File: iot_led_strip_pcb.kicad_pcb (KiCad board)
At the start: 2 copper layers, 50 x 50 mm, 61 parts, among them J1 I2C Expansion, J2 Conn_01x03_Socket, J3 GT-USB-7010ASV, J4 Barrel_Jack_Switch_Pin3Ring, J5 TC2050-IDC_Cortex-M, J6 Conn_01x03_Socket_Solderwire, Q1 BSS138, SW1 RESET, SW2 FLASH, U1 AMS1117-3.3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

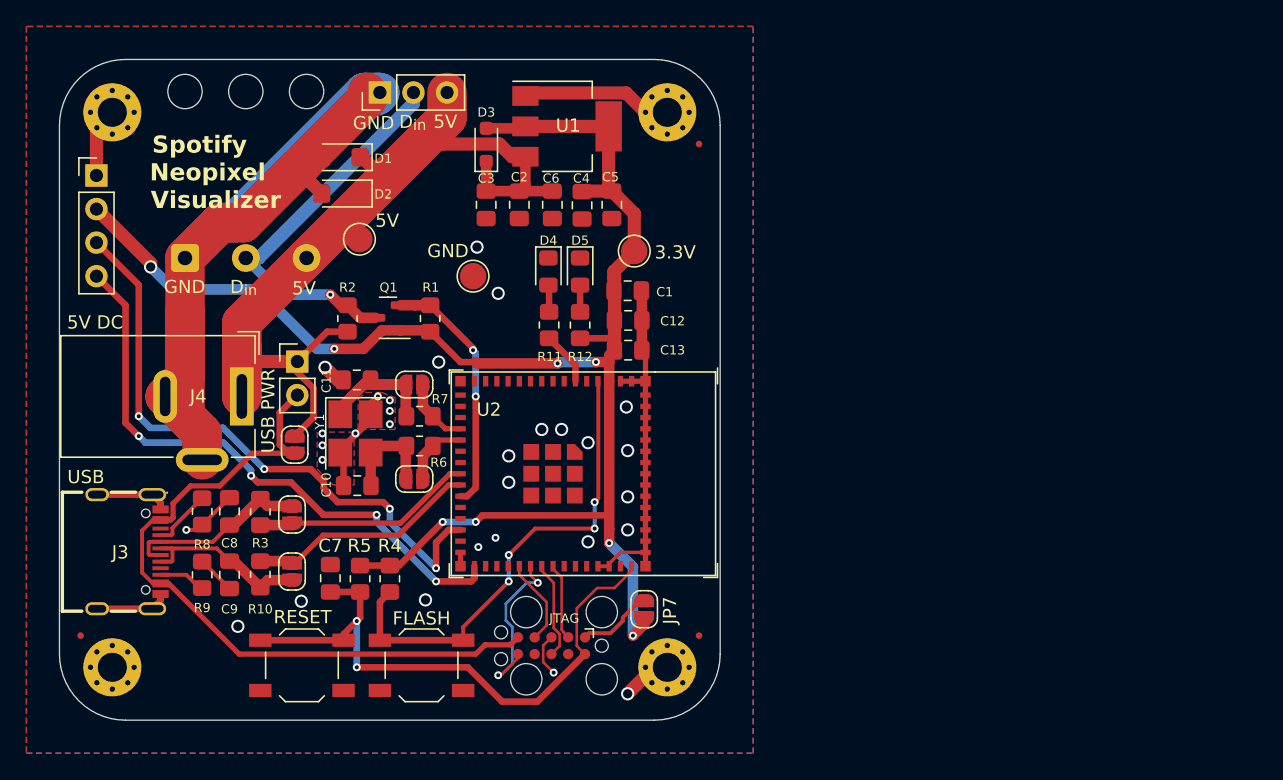
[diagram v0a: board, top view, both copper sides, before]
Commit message: some minor cleanup of schematic and layout
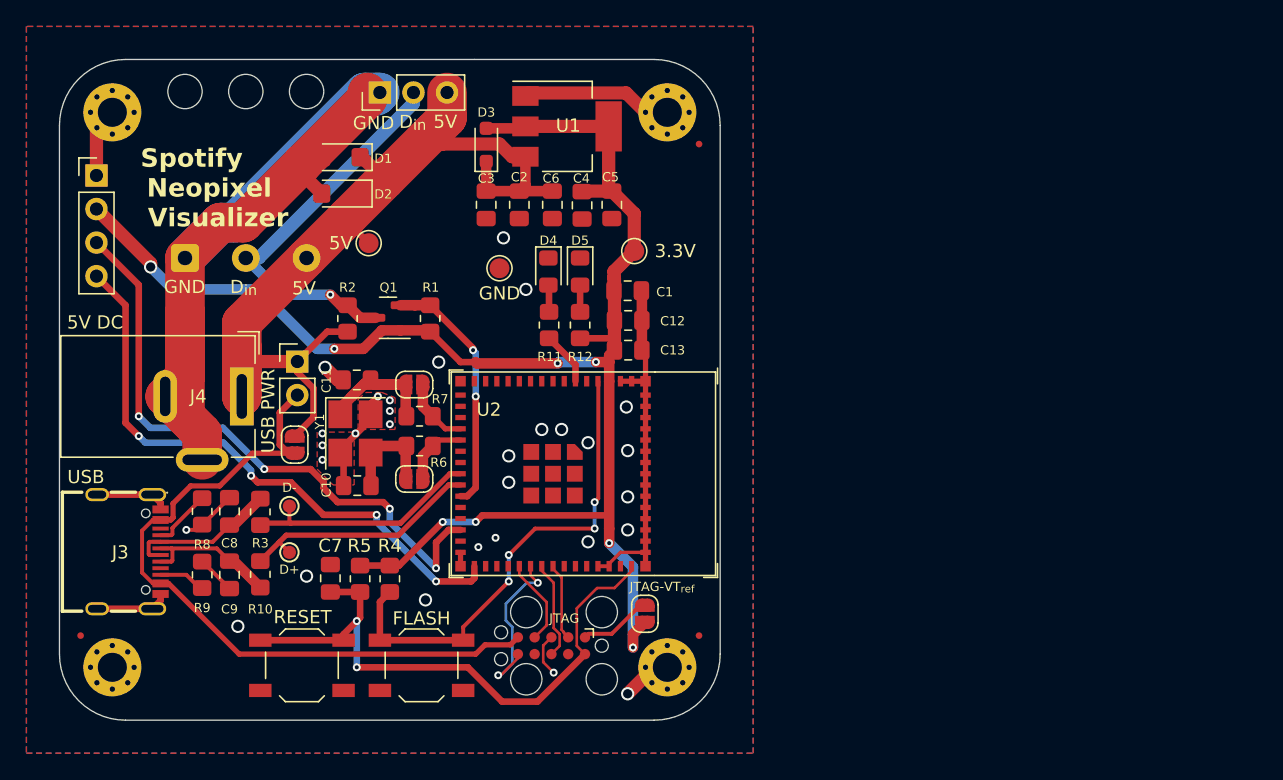
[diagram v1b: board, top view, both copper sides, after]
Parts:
- removed JP2, JP5: SolderJumper_2_Open, Jumper:SolderJumper-2_P1.3mm_Open_RoundedPad1.0x1.5mm
- added TP4: D+, TestPoint:TestPoint_Pad_D1.0mm, F.Cu at (127.4, 107.3)
- added TP5: D-, TestPoint:TestPoint_Pad_D1.0mm, F.Cu at (127.4, 103.8)
- JP7: value JTAG-VTREF -> JTAG-VT_{ref}
- TP1, TP2, TP3: footprint TestPoint:TestPoint_Pad_D2.0mm -> TestPoint:TestPoint_Pad_D1.5mm
- moved TP3 2.09 mm to (143.3, 85.8)
- moved TP1 0.76 mm to (133.4, 83.9)
- moved JP7 0.35 mm to (154.3, 112.0)
- moved REF** 0.28 mm to (123.8, 115.8)
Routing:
- net /DP: track 13.6 -> 10.7 mm
- net /DN: track 14.4 -> 11.6 mm
- net +5V: track 69.7 -> 72.4 mm
- net +3.3V: track 128.8 -> 130.2 mm
- net /USB_D-: track 16.8 -> 18.1 mm
- net /USB_D+: track 17.7 -> 18.6 mm

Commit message: final modifications, cleanup, added v2.0 photos as ordered
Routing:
- net Earth: track 146.6 -> 151.6 mm
- net +5V: track 72.4 -> 75.4 mm
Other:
- board text added: "JTAG VT_{ref}"
- board text added: "v2.0 09-2023"
- board text removed: "v2.0-a 09-2023"

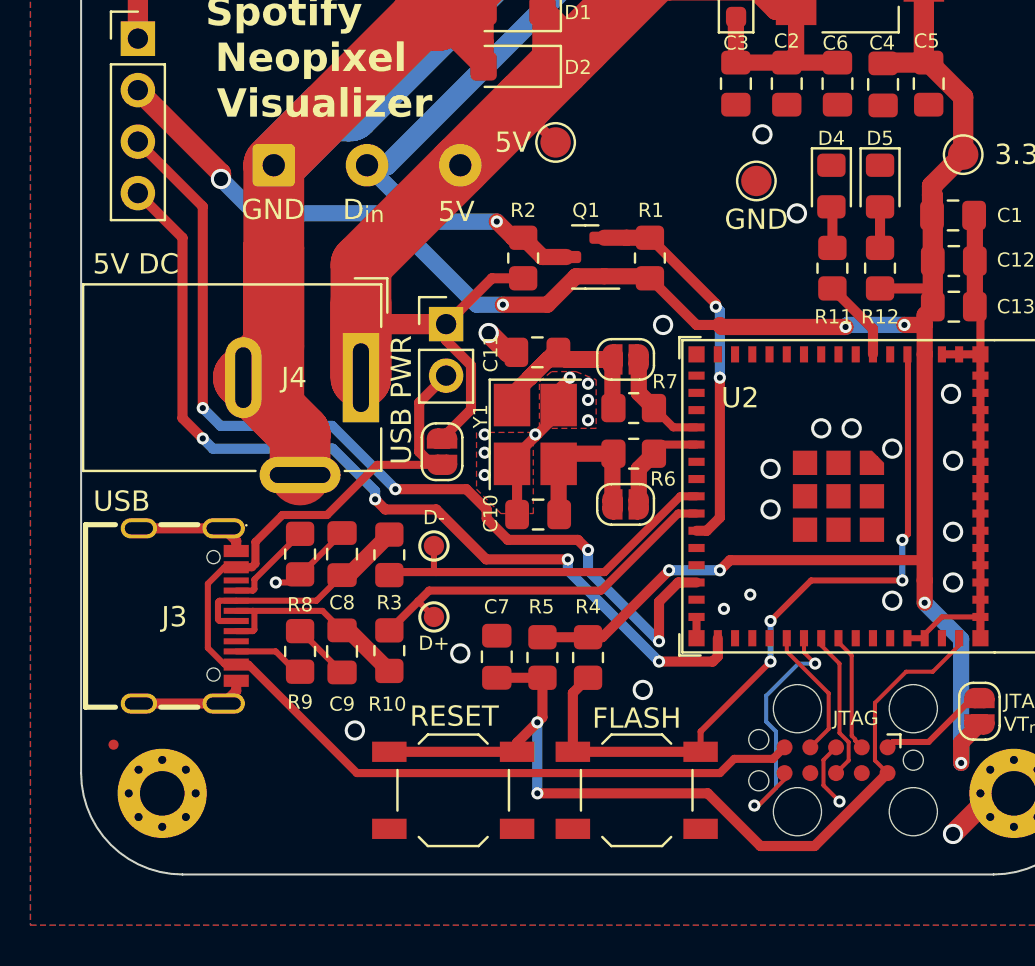
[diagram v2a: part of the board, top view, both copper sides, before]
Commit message: Moved button labels and multiple minor modifications
* Implemented Orion's suggestion for replacing 10uF cap on reset button
  with 100nF.
* Moved silkscreen for both buttons underneath and moved jtag label.
* Added labels to both power and status LEDs.
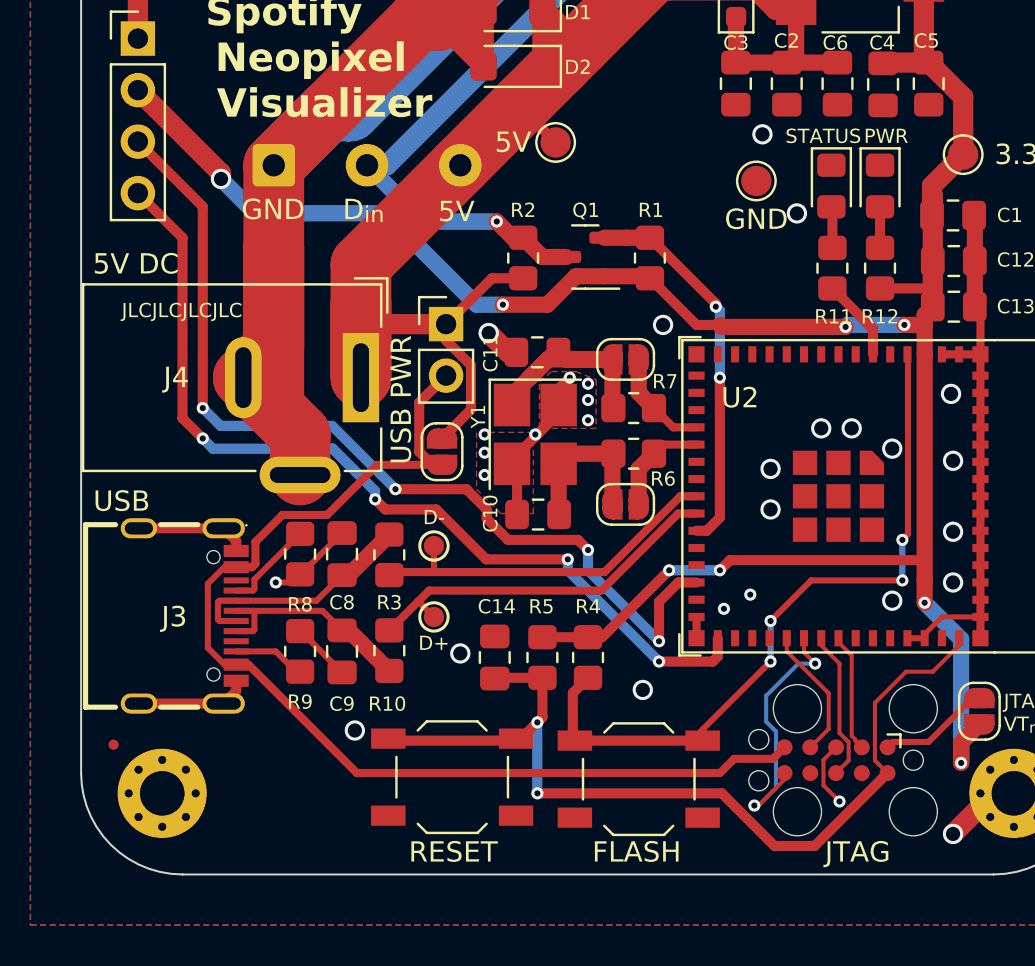
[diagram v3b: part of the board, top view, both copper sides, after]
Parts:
- removed C7: 10uF, Capacitor_SMD:C_0805_2012Metric_Pad1.18x1.45mm_HandSolder
- removed REF**: KiCad-Logo2_5mm_SilkScreen, Symbol:KiCad-Logo2_5mm_SilkScreen
- added C14: 100nF, Capacitor_SMD:C_0805_2012Metric_Pad1.18x1.45mm_HandSolder, F.Cu at (130.4, 109.3)
- D4: value LED -> STATUS
- D5: value PWR_LED -> PWR
- moved SW1 0.65 mm to (128.3, 115.2)
- moved SW2 0.56 mm to (137.5, 115.3)
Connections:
- net /BOOT renamed BOOT
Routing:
- net BOOT: track 36.7 -> 34.9 mm
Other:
- board text added: "JLCJLCJLCJLC"

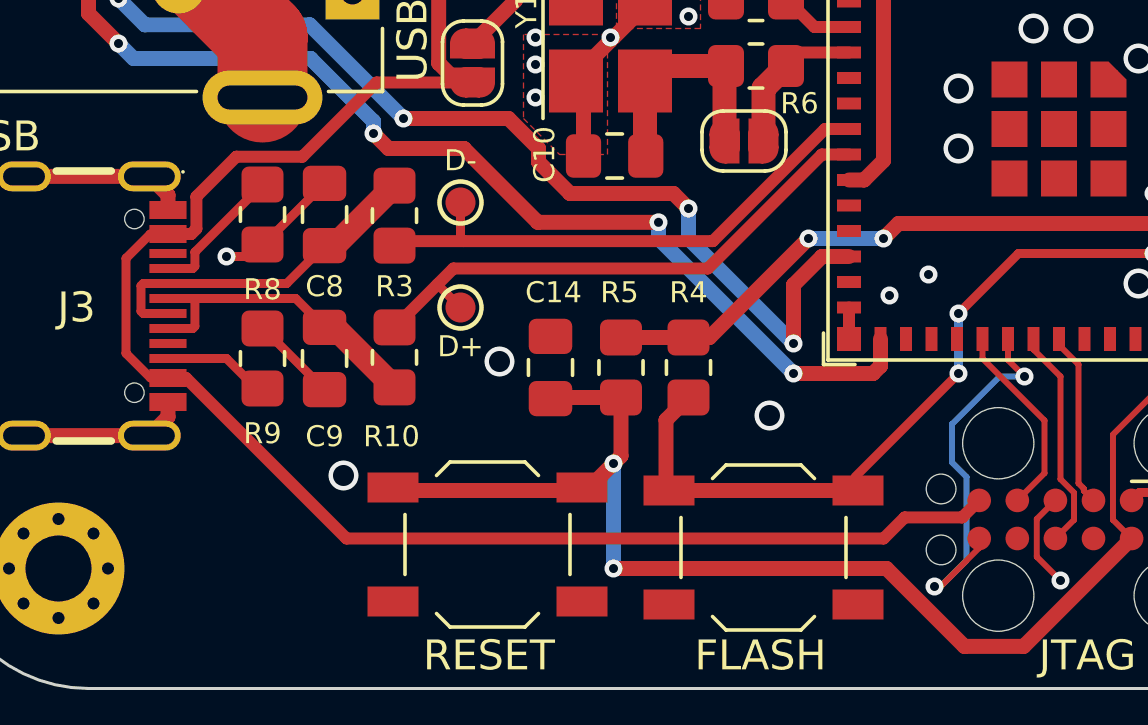
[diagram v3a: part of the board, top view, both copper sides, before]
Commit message: some pcb changes and update to readme
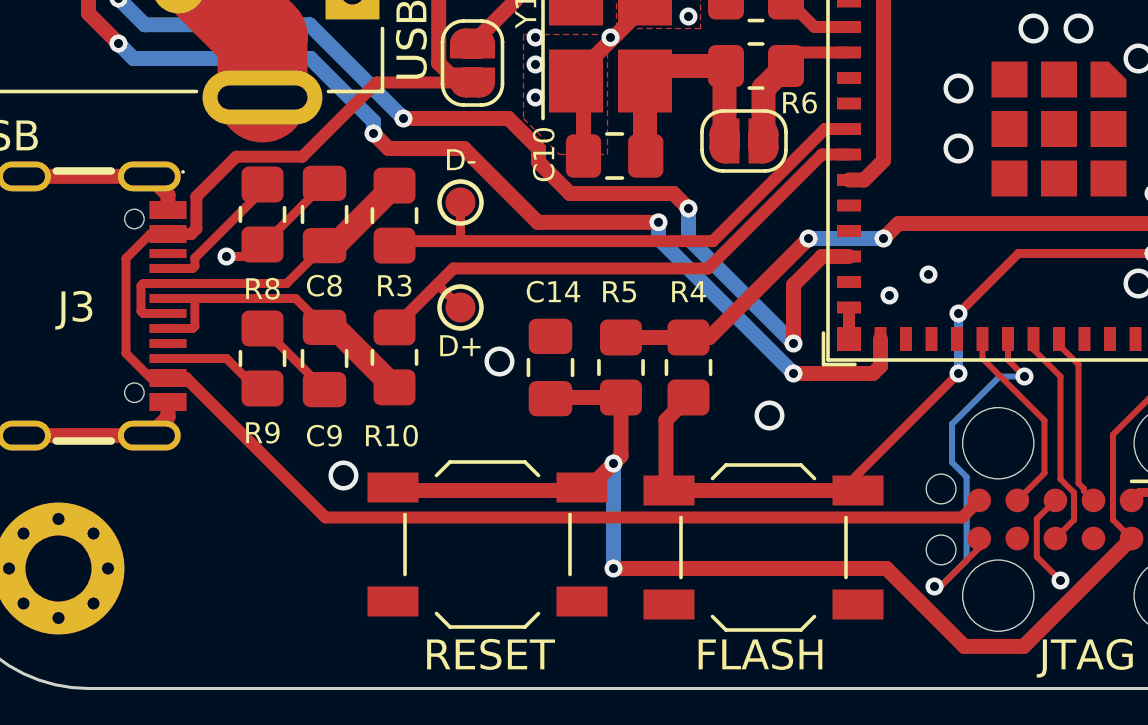
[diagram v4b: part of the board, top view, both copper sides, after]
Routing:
- net VBUS: track 55.0 -> 54.4 mm
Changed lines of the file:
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@@
     (property "Vendor" "https://www.lcsc.com/product-detail/USB-Connectors_G-Switch-GT-USB-7010ASV_C2988369.html")
     (property "ki_keywords" "C2988369")
+    (clearance 0.1)
     (attr smd)
     (fp_text reference "J3" (at 0.05 0.65) (layer "F.SilkS")
@@
     (fp_circle (center 2.889992 -1.280137) (end 3.014986 -1.280137)
       (stroke (width 0.250012) (type solid)) (fill none) (layer "F.Fab"))
-    (pad "" np_thru_hole circle (at -2.899949 -1.280137 270) (size 0.649987 0.649987) (drill 0.649987) (layers "*.Cu" "*.Mask"))
+    (pad "" np_thru_hole circle (at -2.899949 -1.280137 270) (size 0.649987 0.649987) (drill 0.649987) (layers "F&B.Cu" "*.Mask")
+      (clearance 0.1))
     (pad "" np_thru_hole circle (at 2.889992 -1.280137 270) (size 0.649987 0.649987) (drill 0.649987) (layers "*.Cu" "*.Mask"))
     (pad "1" thru_hole oval (at -4.320066 -1.78001 270) (size 1 2.1) (drill oval 0.6 1.7) (layers "*.Cu" "*.Mask")
@@
   (via (at 132.5 112.5) (size 0.6) (drill 0.3) (layers "F.Cu" "B.Cu") (net 6))
   (segment (start 132.5 112.5) (end 132.5 116) (width 0.5) (layer "B.Cu") (net 6))
+  (segment (start 118.250025 109.650025) (end 117.650025 109.650025) (width 0.4) (layer "F.Cu") (net 7))
   (segment (start 127.8 99.8) (end 124.602749 99.8) (width 0.4) (layer "F.Cu") (net 7))
   (segment (start 119.927 102.273) (end 118.597027 103.602973) (width 0.4) (layer "F.Cu") (net 7))
   (segment (start 117.650025 109.650025) (end 117.071123 109.650025) (width 0.3) (layer "F.Cu") (net 7))
-  (segment (start 144.69 113.73) (end 144.1217 114.2983) (width 0.4) (layer "F.Cu") (net 7))
   (segment (start 118.597027 104.677076) (end 118.424179 104.849924) (width 0.4) (layer "F.Cu") (net 7))
-  (segment (start 142.2057 114.2983) (end 141.504 115) (width 0.4) (layer "F.Cu") (net 7))
   (segment (start 117.061217 104.849924) (end 117.650025 104.849924) (width 0.3) (layer "F.Cu") (net 7))
   (segment (start 116.25 108.828902) (end 116.25 105.661141) (width 0.3) (layer "F.Cu") (net 7))
-  (segment (start 144.1217 114.2983) (end 142.2057 114.2983) (width 0.4) (layer "F.Cu") (net 7))
+  (segment (start 122.8983 114.2983) (end 118.250025 109.650025) (width 0.4) (layer "F.Cu") (net 7))
+  (segment (start 144.69 113.73) (end 144.1217 114.2983) (width 0.4) (layer "F.Cu") (net 7))
   (segment (start 117.071123 109.650025) (end 116.25 108.828902) (width 0.3) (layer "F.Cu") (net 7))
   (segment (start 126.673 96.727) (end 126.673 99.15616) (width 0.5) (layer "F.Cu") (net 7))
@@
   (segment (start 126.673 99.15616) (end 127.31684 99.8) (width 0.5) (layer "F.Cu") (net 7))
   (segment (start 116.25 105.661141) (end 117.061217 104.849924) (width 0.3) (layer "F.Cu") (net 7))
-  (segment (start 123.6 115) (end 118.250025 109.650025) (width 0.4) (layer "F.Cu") (net 7))
   (segment (start 124.602749 99.8) (end 122.129749 102.273) (width 0.4) (layer "F.Cu") (net 7))
   (segment (start 118.424179 104.849924) (end 117.650025 104.849924) (width 0.4) (layer "F.Cu") (net 7))
-  (segment (start 141.504 115) (end 123.6 115) (width 0.4) (layer "F.Cu") (net 7))
   (segment (start 128 95.4) (end 126.673 96.727) (width 0.5) (layer "F.Cu") (net 7))
-  (segment (start 118.250025 109.650025) (end 117.650025 109.650025) (width 0.4) (layer "F.Cu") (net 7))
+  (segment (start 144.1217 114.2983) (end 122.8983 114.2983) (width 0.4) (layer "F.Cu") (net 7))
   (segment (start 127.31684 99.8) (end 127.8 99.8) (width 0.5) (layer "F.Cu") (net 7))
   (segment (start 132.75 89.55) (end 131.8 88.6) (width 0.8) (layer "F.Cu") (net 8))
@@
   (segment (start 147.05 87.125) (end 147 87.075) (width 0.5) (layer "F.Cu") (net 23))
   (segment (start 149.4 87.075) (end 149.4 89.1) (width 0.5) (layer "F.Cu") (net 24))
-  (segment (start 118.4739 106.000038) (end 118.547027 105.926911) (width 0.3) (layer "F.Cu") (net 25))
-  (segment (start 118.547027 105.452973) (end 120.8 103.2) (width 0.3) (layer "F.Cu") (net 25))
+  (segment (start 120.8 103.4) (end 120.8 103.2) (width 0.3) (layer "F.Cu") (net 25))
   (segment (start 117.650025 106.000038) (end 118.4739 106.000038) (width 0.3) (layer "F.Cu") (net 25))
-  (segment (start 118.547027 105.926911) (end 118.547027 105.452973) (width 0.3) (layer "F.Cu") (net 25))
+  (segment (start 118.547027 105.926911) (end 118.547027 105.652973) (width 0.3) (layer "F.Cu") (net 25))
+  (segment (start 118.547027 105.652973) (end 120.8 103.4) (width 0.3) (layer "F.Cu") (net 25))
+  (segment (start 118.4739 106.000038) (end 118.547027 105.926911) (width 0.3) (layer "F.Cu") (net 25))
   (segment (start 120.6 110) (end 120.8 110) (width 0.3) (layer "F.Cu") (net 27))
   (segment (start 117.650025 109.000038) (end 119.600038 109.000038) (width 0.3) (layer "F.Cu") (net 27))
@@
     (polygon
       (pts
-        (xy 154.5 93.5)
-        (xy 155.1 93.5)
+        (xy 152.2 93.7)
+        (xy 155.1 93.7)
         (xy 155.1 92.9)
-        (xy 154.5 92.9)
+        (xy 152.2 92.9)
       )
     )

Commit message: small modifications + RT render
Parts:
- added REF**: KiCad-Logo2_5mm_SilkScreen, Symbol:KiCad-Logo2_5mm_SilkScreen, B.Cu at (123.7, 115.9)
- D4: value STATUS -> STAT
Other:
- board text added: "M2 Mounting Holes"
- board text added: "Tag-Connect JTAG Header"

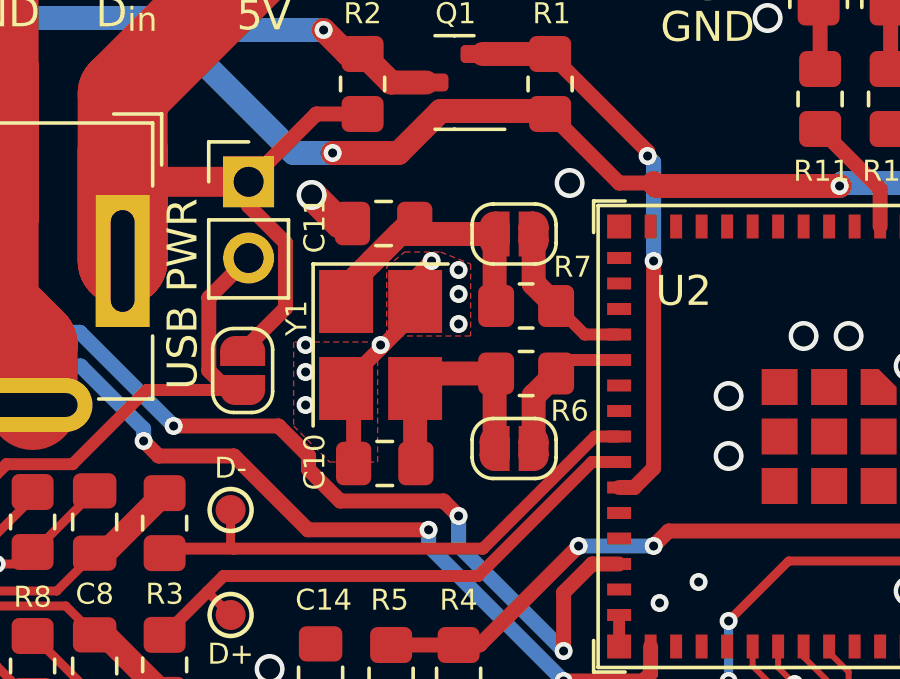
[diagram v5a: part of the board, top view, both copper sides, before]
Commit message: PCBA today - field edits on Cs, Rs, removed Rs on Y1
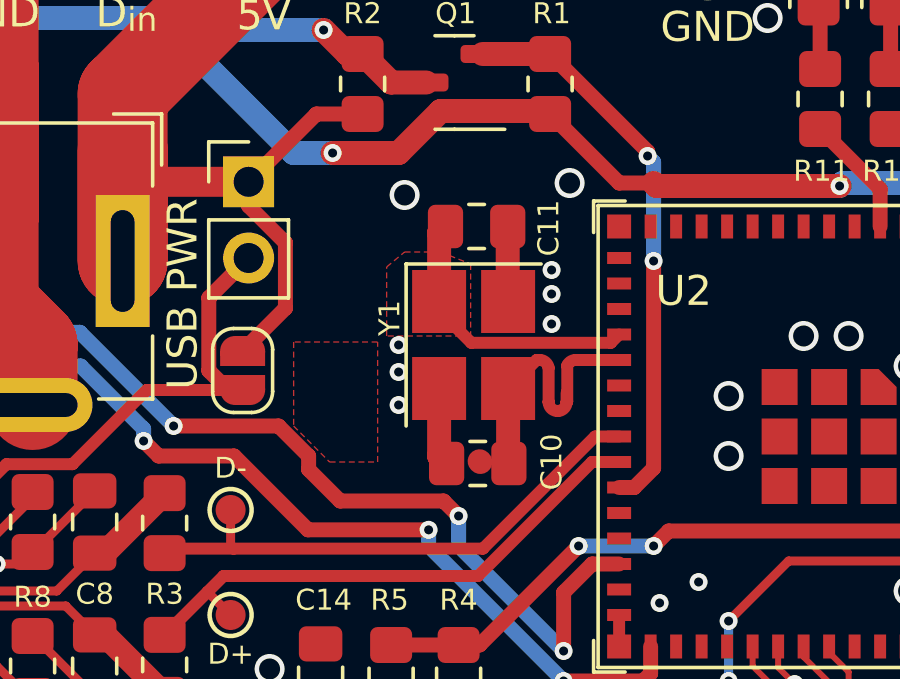
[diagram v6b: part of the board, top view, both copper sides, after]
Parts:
- removed JP1, JP6: SolderJumper_2_Open, Jumper:SolderJumper-2_P1.3mm_Open_RoundedPad1.0x1.5mm
- removed R6, R7: 0R, Resistor_SMD:R_0805_2012Metric_Pad1.20x1.40mm_HandSolder
- Y1: value Crystal_40Mhz -> Crystal_32Mhz
- moved C11 3.10 mm to (135.6, 94.3), turned to 0 degrees
- moved C10 3.10 mm to (135.6, 102.2)
- moved Y1 3.10 mm to (135.5, 98.3)
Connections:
- C10 pad 1: /X1_R -> /XN
- C11 pad 1: /X0_R -> /XP
- U2 pad 19: /X0 -> /XP
- U2 pad 20: /X1 -> /XN
- Y1 pad 1: /X0_R -> /XP
- Y1 pad 3: /X1_R -> /XN
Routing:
- net /X0_R: track 13.3 -> 0.00 mm
- net /XN: track 0.00 -> 10.5 mm
- net /XP: track 0.00 -> 9.45 mm
- net /X1_R: track 7.94 -> 0.00 mm
- net /X0: track 5.70 -> 0.00 mm
- net /X1: track 5.10 -> 0.00 mm
- net Earth: track 151.6 -> 147.0 mm, vias 30 -> 28
